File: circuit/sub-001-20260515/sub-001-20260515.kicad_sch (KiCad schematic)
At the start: 93 parts, among them J1 Conn_Main, J2 Conn_NeoPixel, J3 Conn_SW_TGL, J4 Conn_Power, Q1 NMOS, Q2 NMOS, Q3 NMOS, Q4 NMOS, U1 LM1117MP-3.3, U10 LM1117MP-3.3, U11 LM1117MP-3.3, U12 LM1117MP-3.3, U13 LM1117MP-3.3, U14 TSSP58038, U15 TSSP58038, U16 TSSP58038, U17 TSSP58038, U18 NE555P, U19 NE555P, U20 NE555P, U21 NE555P, U9 LM1117MP-3.3

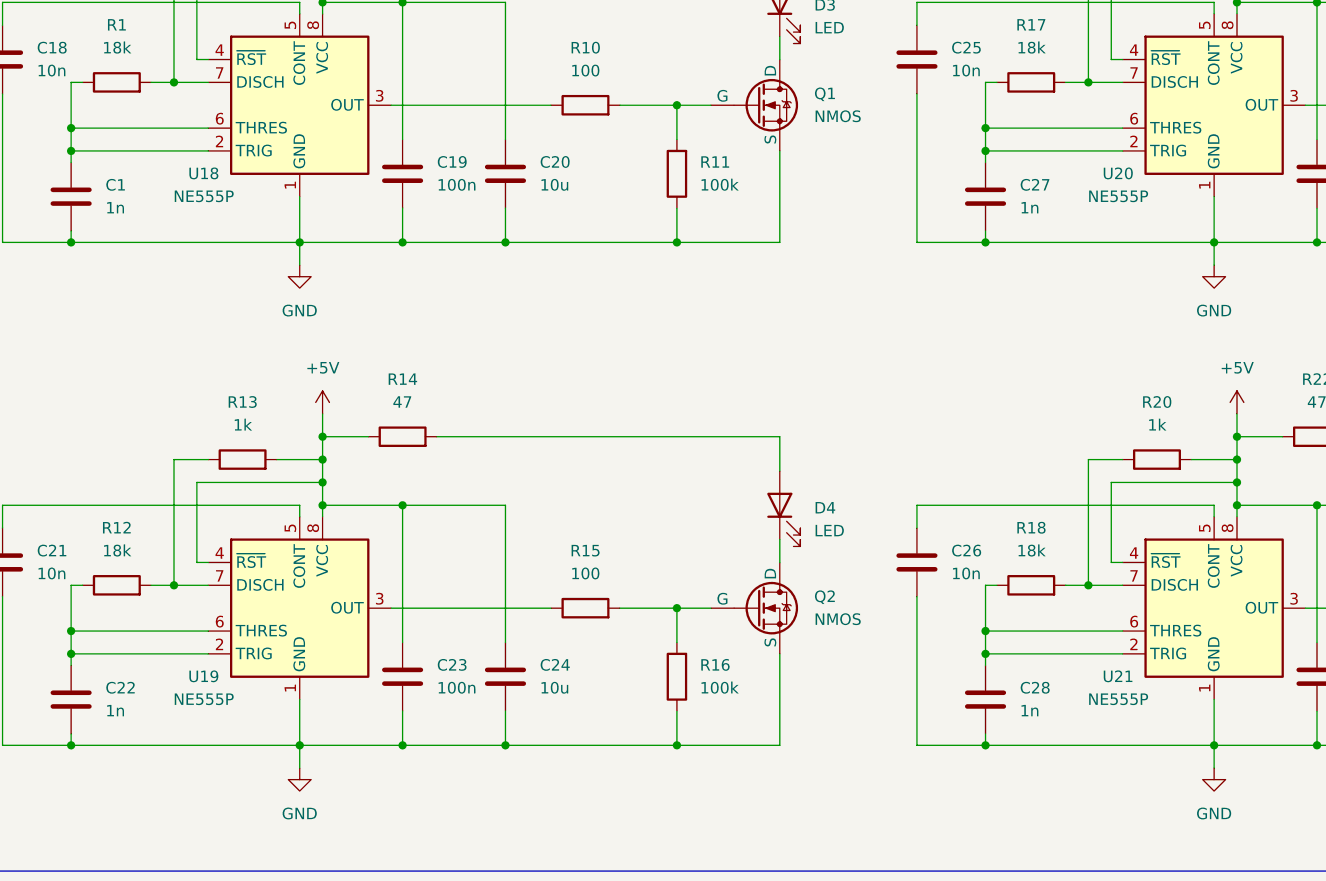
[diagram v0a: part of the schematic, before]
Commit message: Update サブ基板のタイマーICをNE555PからNe555DRに変更
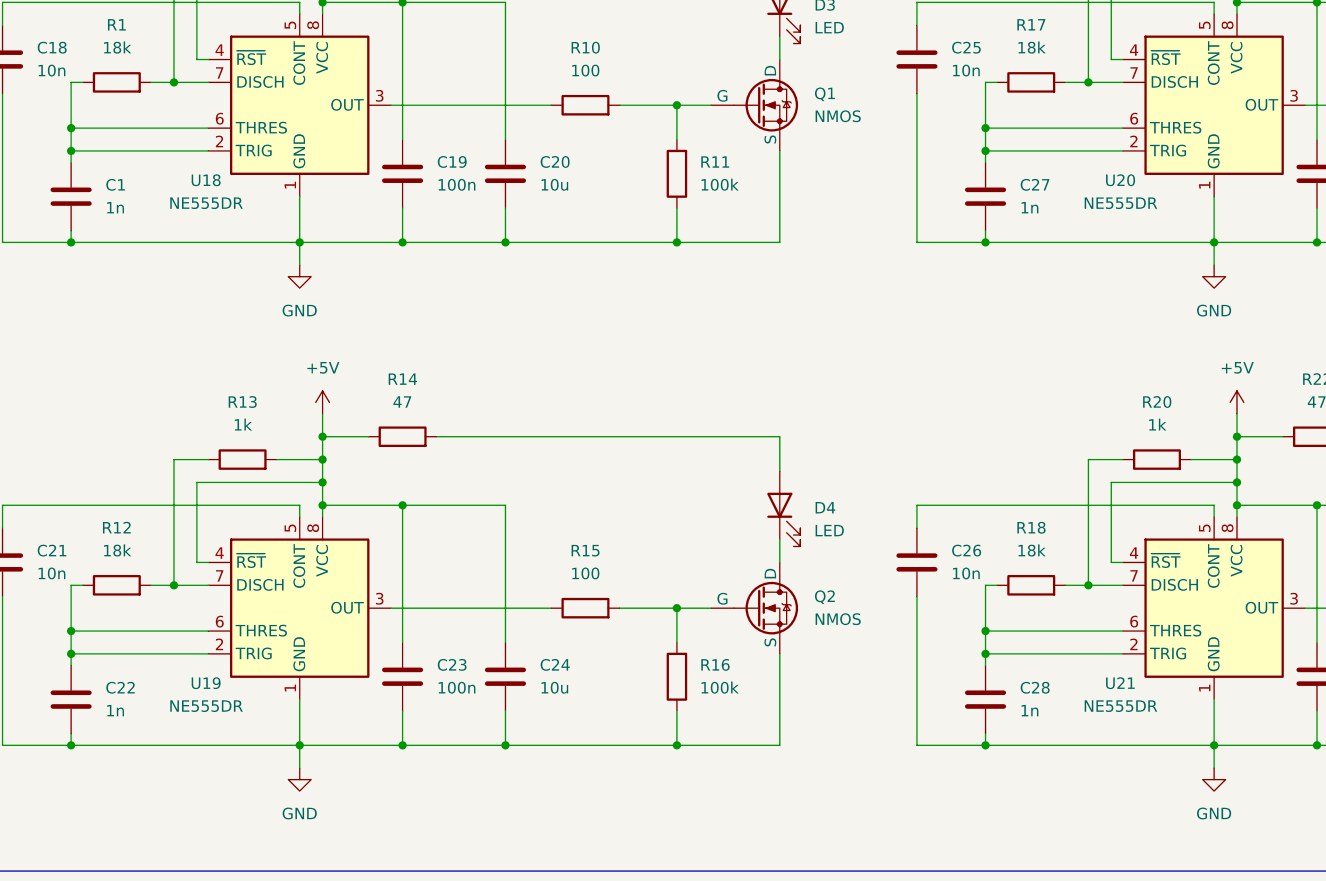
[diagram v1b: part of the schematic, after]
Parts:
- removed U18, U19, U20, U21: NE555P, Package_DIP:DIP-8_W7.62mm, symbol Timer:NE555P
- added U18, U19, U20, U21: NE555DR, Package_SO:SOIC-8_3.9x4.9mm_P1.27mm, symbol Timer:NE555D
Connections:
- net +5V: now also U18.4 (~{RST}), U18.8 (VCC), U19.4 (~{RST}), U19.8 (VCC), U20.4 (~{RST}), U20.8 (VCC), U21.4 (~{RST}), U21.8 (VCC)
- net GND: now also U18.1 (GND), U19.1 (GND), U20.1 (GND), U21.1 (GND)
- net at R12.2, R13.1: now also U19.7 (DISCH)
- net at R24.1: now also U21.3 (OUT)
- net at C25.2: now also U20.5 (CONT)
- net at R23.1: now also U20.3 (OUT)
- net at C27.1, R17.1: now also U20.2 (TRIG), U20.6 (THRES)
- net at R17.2, R19.1: now also U20.7 (DISCH)
- net at R15.1: now also U19.3 (OUT)
- net at R1.2, R2.1: now also U18.7 (DISCH)
- net at R10.1: now also U18.3 (OUT)
- net at R18.2, R20.1: now also U21.7 (DISCH)
- net at C26.2: now also U21.5 (CONT)
- net at C1.1, R1.1: now also U18.2 (TRIG), U18.6 (THRES)
- net at C28.1, R18.1: now also U21.2 (TRIG), U21.6 (THRES)
- net at C18.2: now also U18.5 (CONT)
- net at C22.1, R12.1: now also U19.2 (TRIG), U19.6 (THRES)
- net at C21.2: now also U19.5 (CONT)

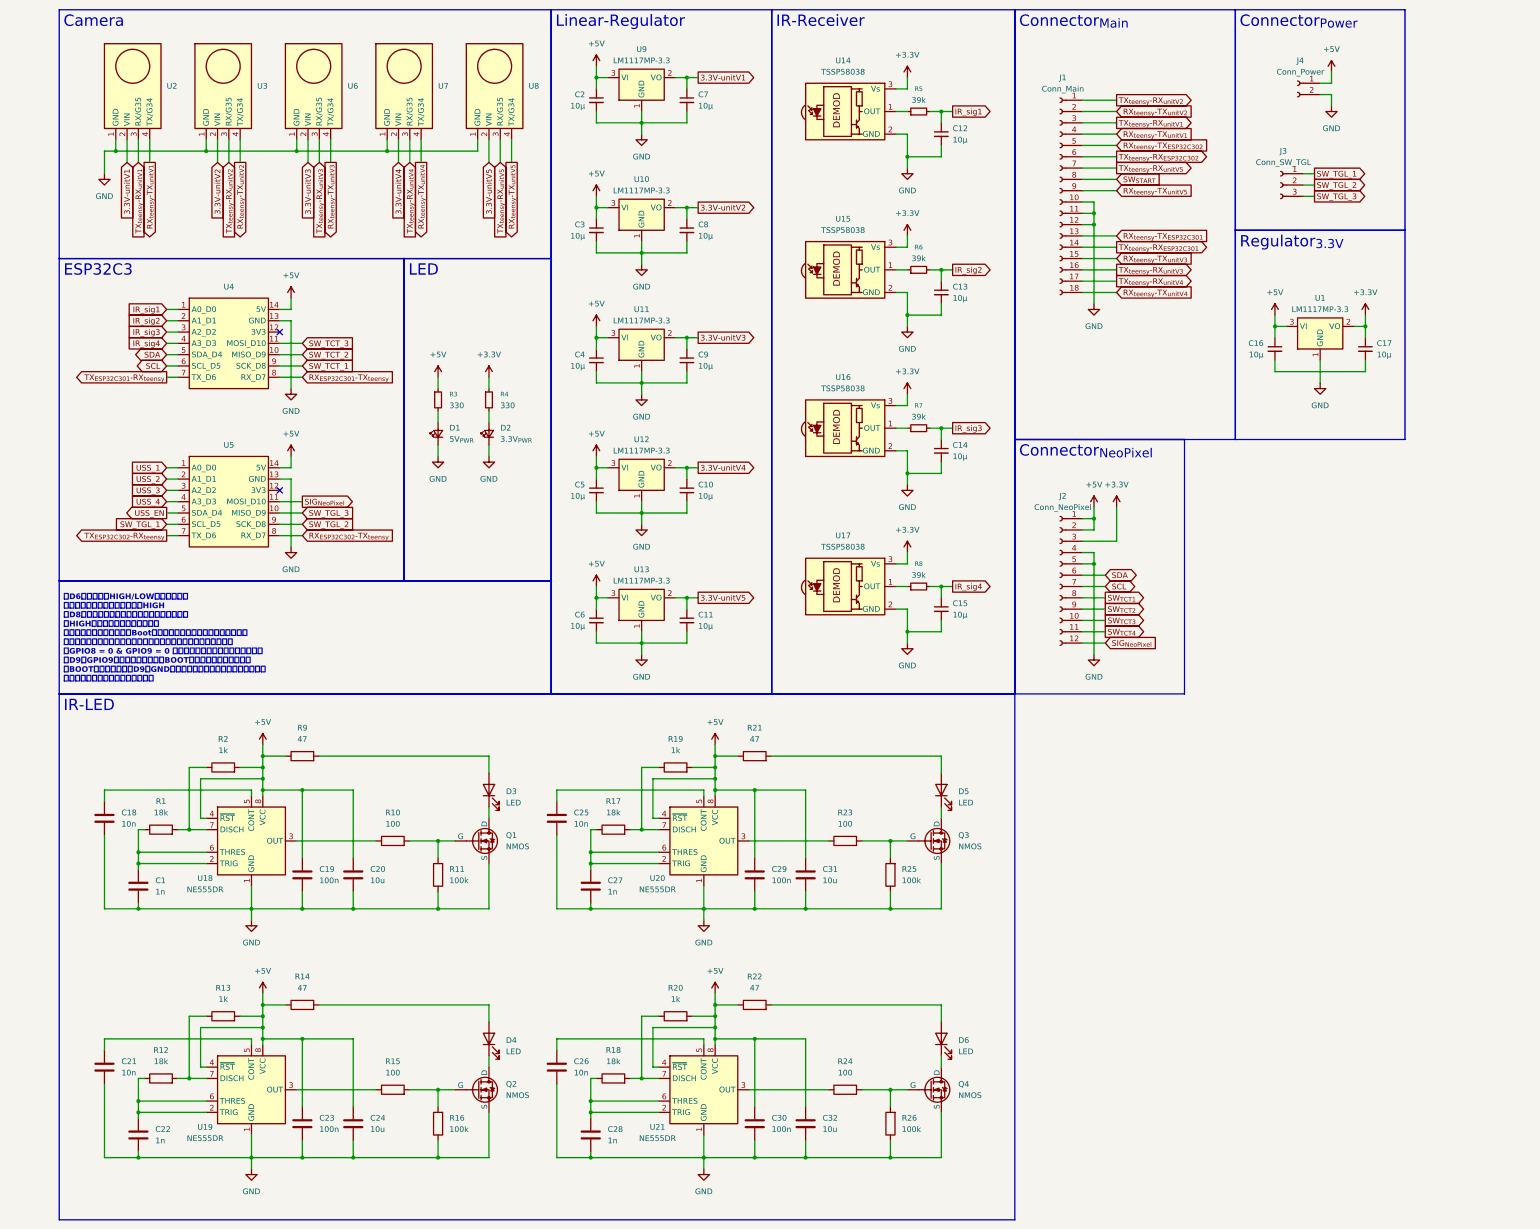
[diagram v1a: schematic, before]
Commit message: Update サブ基板の回路図を更新
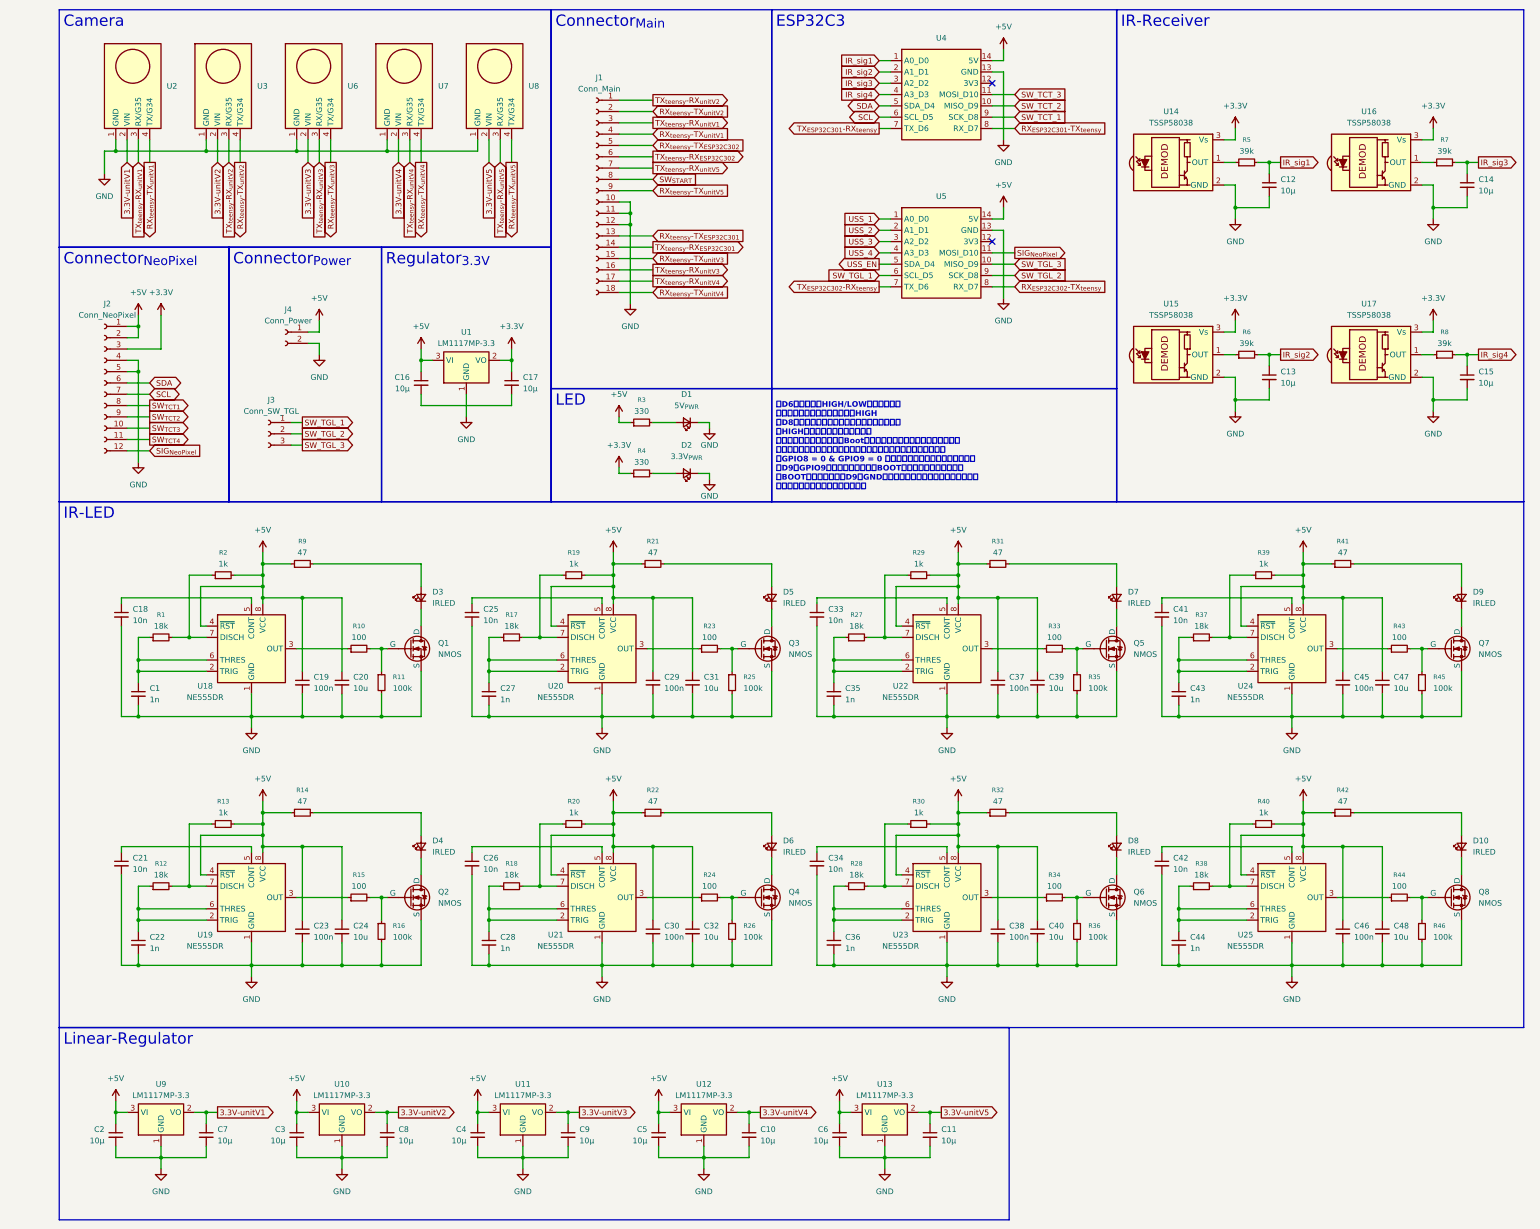
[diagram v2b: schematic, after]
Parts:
- removed C1, C22, C27, C28: 1n, symbol Device:C
- removed C18, C21, C25, C26: 10n, symbol Device:C
- removed C19, C23, C29, C30: 100n, symbol Device:C
- removed C20, C24, C31, C32: 10u, symbol Device:C
- removed D3, D4, D5, D6: LED, symbol Device:LED
- removed R1, R12, R17, R18: 18k, symbol Device:R
- removed R10, R15, R23, R24: 100, symbol Device:R
- removed R11, R16, R25, R26: 100k, symbol Device:R
- removed R13, R19, R2, R20: 1k, symbol Device:R
- removed R14, R21, R22, R9: 47, symbol Device:R
- added C1, C22, C27, C28, C35, C36, C43, C44: 1n, symbol Device:C_Small
- added C18, C21, C25, C26, C33, C34, C41, C42: 10n, symbol Device:C_Small
- added C19, C23, C29, C30, C37, C38, C45, C46: 100n, symbol Device:C_Small
- added C20, C24, C31, C32, C39, C40, C47, C48: 10u, symbol Device:C_Small
- added D10, D3, D4, D5, D6, D7, D8, D9: IRLED, symbol Device:LED_Small
- added Q5, Q6, Q7, Q8: NMOS, symbol Simulation_SPICE:NMOS
- added R1, R12, R17, R18, R27, R28, R37, R38: 18k, symbol Device:R_Small
- added R10, R15, R23, R24, R33, R34, R43, R44: 100, symbol Device:R_Small
- added R11, R16, R25, R26, R35, R36, R45, R46: 100k, symbol Device:R_Small
- added R13, R19, R2, R20, R29, R30, R39, R40: 1k, symbol Device:R_Small
- added R14, R21, R22, R31, R32, R41, R42, R9: 47, symbol Device:R_Small
- added U22, U23, U24, U25: NE555DR, Package_SO:SOIC-8_3.9x4.9mm_P1.27mm, symbol Timer:NE555D
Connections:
- net +5V: now also C19.1, C20.1, C23.1, C24.1, C29.1, C30.1, C31.1, C32.1, C37.1, C38.1, C39.1, C40.1, C45.1, C46.1, C47.1, C48.1, R13.2, R14.1, R19.2, R2.2, R20.2, R21.1, R22.1, R29.2, R30.2, R31.1, R32.1, R39.2, R40.2, R41.1, R42.1, R9.1, U22.4 (~{RST}), U22.8 (VCC), U23.4 (~{RST}), U23.8 (VCC), U24.4 (~{RST}), U24.8 (VCC), U25.4 (~{RST}), U25.8 (VCC)
- net GND: now also C1.2, C18.2, C19.2, C20.2, C21.2, C22.2, C23.2, C24.2, C25.2, C26.2, C27.2, C28.2, C29.2, C30.2, C31.2, C32.2, C33.2, C34.2, C35.2, C36.2, C37.2, C38.2, C39.2, C40.2, C41.2, C42.2, C43.2, C44.2, C45.2, C46.2, C47.2, C48.2, Q5.3 (S), Q6.3 (S), Q7.3 (S), Q8.3 (S), R11.2, R16.2, R25.2, R26.2, R35.2, R36.2, R45.2, R46.2, U22.1 (GND), U23.1 (GND), U24.1 (GND), U25.1 (GND)
- net at U19.7 (DISCH): now also R12.2, R13.1
- net at Q2.1 (D): now also D4.1 (K)
- net at Q2.2 (G): now also R15.2, R16.1
- net at Q3.1 (D): now also D5.1 (K)
- net at U21.3 (OUT): now also R24.1
- net at Q4.2 (G): now also R24.2, R26.1
- net at U21.2 (TRIG), U21.6 (THRES): now also C28.1, R18.1
- net at U21.5 (CONT): now also C26.1
- net at U21.7 (DISCH): now also R18.2, R20.1
- net at Q1.2 (G): now also R10.2, R11.1
- net at U20.5 (CONT): now also C25.1
- net at U20.3 (OUT): now also R23.1
- net at Q3.2 (G): now also R23.2, R25.1
- net at U18.2 (TRIG), U18.6 (THRES): now also C1.1, R1.1
- net at U18.3 (OUT): now also R10.1
- net at U18.5 (CONT): now also C18.1
- net at U18.7 (DISCH): now also R1.2, R2.1
- net at U20.2 (TRIG), U20.6 (THRES): now also C27.1, R17.1
- net at U20.7 (DISCH): now also R17.2, R19.1
- net at U19.3 (OUT): now also R15.1
- net at Q4.1 (D): now also D6.1 (K)
- net at Q1.1 (D): now also D3.1 (K)
- net at U19.2 (TRIG), U19.6 (THRES): now also C22.1, R12.1
- net at U19.5 (CONT): now also C21.1
- new net: C43.1, R37.1, U24.2 (TRIG), U24.6 (THRES)
- new net: R43.1, U24.3 (OUT)
- new net: C41.1, U24.5 (CONT)
- new net: R37.2, R39.1, U24.7 (DISCH)
- new net: Q7.2 (G), R43.2, R45.1
- new net: D10.1 (K), Q8.1 (D)
- new net: D10.2 (A), R42.2
- new net: Q5.2 (G), R33.2, R35.1
- new net: D7.1 (K), Q5.1 (D)
- new net: D7.2 (A), R31.2
- new net: R28.2, R30.1, U23.7 (DISCH)
- new net: D8.1 (K), Q6.1 (D)
- new net: Q6.2 (G), R34.2, R36.1
- new net: C44.1, R38.1, U25.2 (TRIG), U25.6 (THRES)
- new net: C35.1, R27.1, U22.2 (TRIG), U22.6 (THRES)
- new net: R33.1, U22.3 (OUT)
- new net: C33.1, U22.5 (CONT)
- new net: R27.2, R29.1, U22.7 (DISCH)
- new net: D6.2 (A), R22.2
- new net: Q8.2 (G), R44.2, R46.1
- new net: R38.2, R40.1, U25.7 (DISCH)
- new net: C36.1, R28.1, U23.2 (TRIG), U23.6 (THRES)
- new net: R34.1, U23.3 (OUT)
- new net: C34.1, U23.5 (CONT)
- new net: D3.2 (A), R9.2
- new net: D9.1 (K), Q7.1 (D)
- new net: D5.2 (A), R21.2
- new net: D4.2 (A), R14.2
- new net: D8.2 (A), R32.2
- new net: R44.1, U25.3 (OUT)
- new net: C42.1, U25.5 (CONT)
- new net: D9.2 (A), R41.2
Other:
- moved on the sheet: C10, C11, C12, C13, C14, C15, C16, C17, C2, C3, C4, C5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
